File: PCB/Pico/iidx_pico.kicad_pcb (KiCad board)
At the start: 2 copper layers, 180 x 160 mm, 93 parts, among them J1 Spin, J2 Spin, J3 RGB, J4 RGB, J5 Spin, J6 Spin, SW1 SWITCH_SPST, SW10 SWITCH_SPST, SW11 SWITCH_SPST, SW12 Tact_4pin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

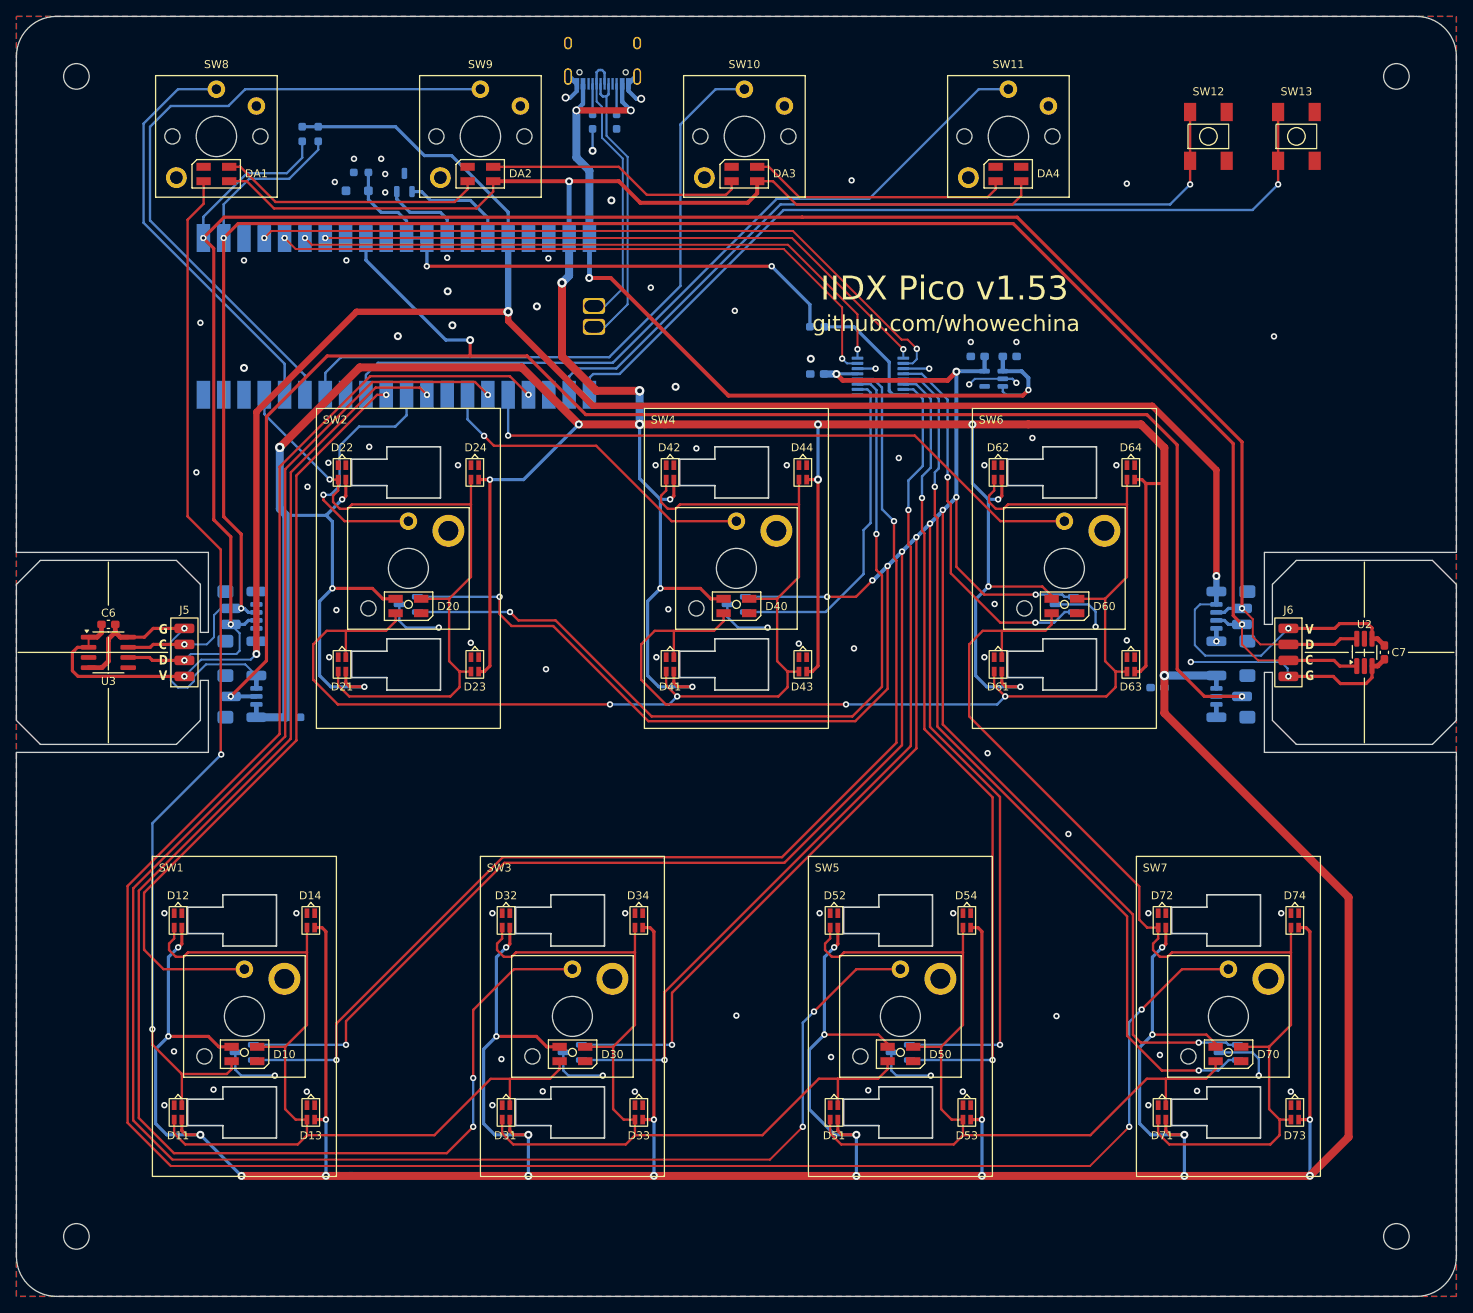
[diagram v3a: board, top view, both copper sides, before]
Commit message: PCB 1.54 (stab steel clearance)
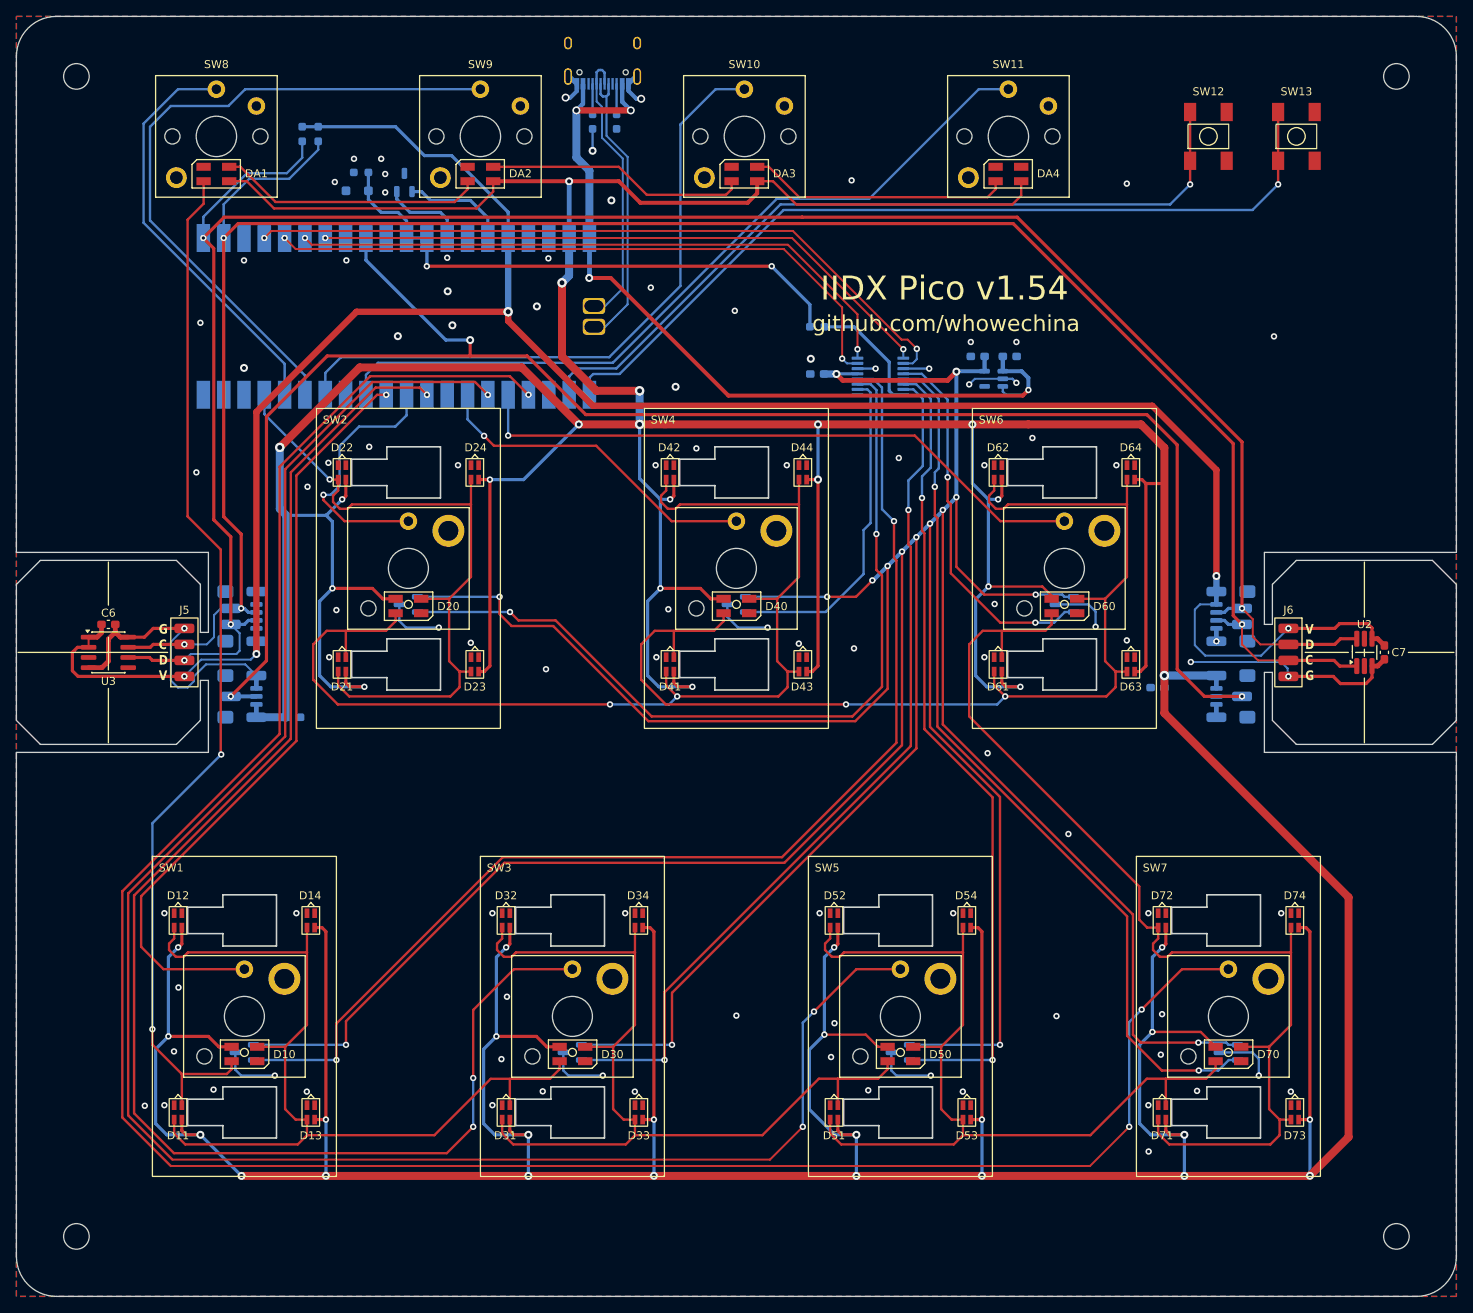
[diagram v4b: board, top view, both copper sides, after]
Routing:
- net Net-(U1-GPIO2): track 284.3 -> 284.9 mm
- net Net-(U1-GPIO4): track 235.2 -> 235.7 mm
- net GND: vias 93 -> 99
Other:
- board text added: "IIDX Pico v1.54"
- board text removed: "IIDX Pico v1.53"

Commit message: Update PCB v1.6 files missed
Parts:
- added JP1: DIR, Jumper:SolderJumper-2_P1.3mm_Open_RoundedPad1.0x1.5mm, F.Cu at (61.9, 94.9)
- moved C6 1.61 mm to (57.2, 95.4)
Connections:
- U3 pad 8: GND -> Net-(JP1-A)
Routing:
- net GND: track 157.2 -> 163.8 mm, vias 99 -> 102
- net Net-(JP1-A): track 0.00 -> 2.09 mm
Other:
- board text added: "IIDX Pico v1.6"
- board text removed: "IIDX Pico v1.54"
